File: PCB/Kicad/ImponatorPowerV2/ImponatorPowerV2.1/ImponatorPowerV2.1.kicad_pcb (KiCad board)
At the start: 6 copper layers, 79 parts, among them IC1 IS31FL3728-QFLS2-TR

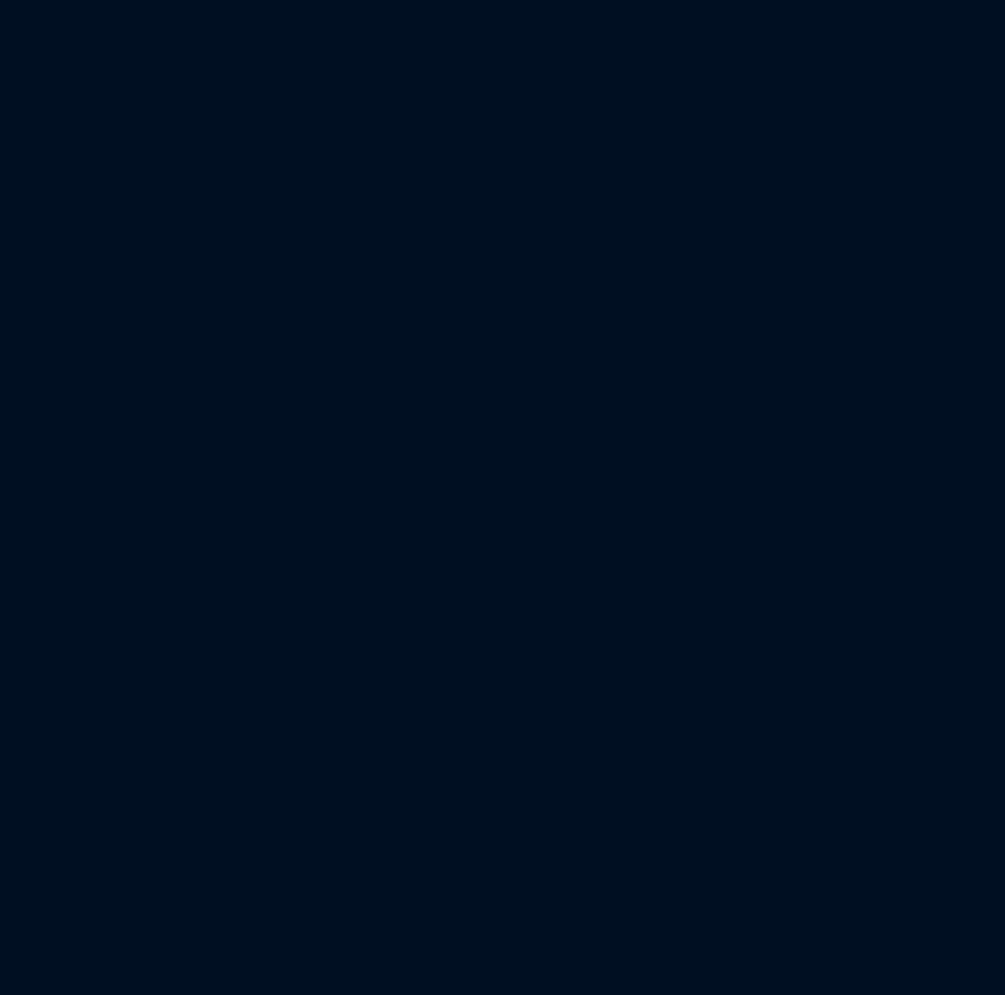
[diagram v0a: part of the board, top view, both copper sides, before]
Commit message: Added components to PCB on V2.1
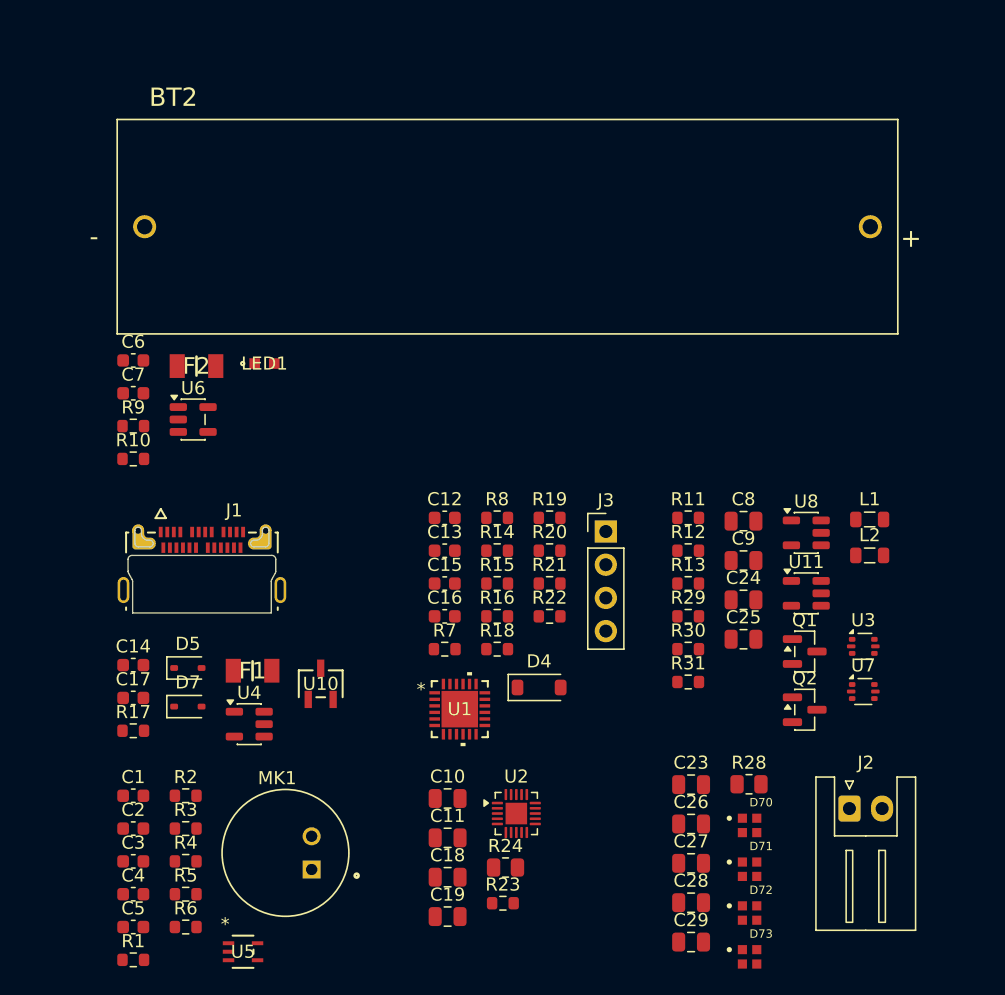
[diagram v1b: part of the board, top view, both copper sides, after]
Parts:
- added BT2: BCAAPC, Custom:BAT_BCAAPC, F.Cu at (94.1, 98.5)
- added C1: 0.1uF, Capacitor_SMD:C_0603_1608Metric, F.Cu at (65.5, 142.0)
- added C10: 4.7uF, Capacitor_SMD:C_0805_2012Metric, F.Cu at (89.5, 142.3)
- added C11: 0.1uF, Capacitor_SMD:C_0805_2012Metric, F.Cu at (89.5, 145.3)
- added C12: 1uF, Capacitor_SMD:C_0603_1608Metric, F.Cu at (89.3, 120.8)
- added C13: 100nF, Capacitor_SMD:C_0603_1608Metric, F.Cu at (89.3, 123.3)
- added C14: 4.7uF, Capacitor_SMD:C_0603_1608Metric, F.Cu at (65.5, 132.1)
- added C15: 1uF, Capacitor_SMD:C_0603_1608Metric, F.Cu at (89.3, 125.8)
- added C16: 1uF, Capacitor_SMD:C_0603_1608Metric, F.Cu at (89.3, 128.3)
- added C17: 1uF, Capacitor_SMD:C_0603_1608Metric, F.Cu at (65.5, 134.6)
- added C18: 4.7uF, Capacitor_SMD:C_0805_2012Metric, F.Cu at (89.5, 148.3)
- added C19: 0.1uF, Capacitor_SMD:C_0805_2012Metric, F.Cu at (89.5, 151.3)
- added C2: 1uF, Capacitor_SMD:C_0603_1608Metric, F.Cu at (65.5, 144.6)
- added C23: 0.1uF, Capacitor_SMD:C_0805_2012Metric, F.Cu at (108.2, 141.2)
- added C24: 4.7uF, Capacitor_SMD:C_0805_2012Metric, F.Cu at (112.2, 127.1)
- added C25: 22uF, Capacitor_SMD:C_0805_2012Metric, F.Cu at (112.2, 130.1)
- added C26: 0.1uF, Capacitor_SMD:C_0805_2012Metric, F.Cu at (108.2, 144.2)
- added C27: 0.1uF, Capacitor_SMD:C_0805_2012Metric, F.Cu at (108.2, 147.2)
- added C28: 0.1uF, Capacitor_SMD:C_0805_2012Metric, F.Cu at (108.2, 150.2)
- added C29: 100uF, Capacitor_SMD:C_0805_2012Metric, F.Cu at (108.2, 153.2)
- added C3: 100pF, Capacitor_SMD:C_0603_1608Metric, F.Cu at (65.5, 147.1)
- added C4: 1uF, Capacitor_SMD:C_0603_1608Metric, F.Cu at (65.5, 149.6)
- added C5: 0.1uF, Capacitor_SMD:C_0603_1608Metric, F.Cu at (65.5, 152.1)
- added C6: 4.7uF, Capacitor_SMD:C_0603_1608Metric, F.Cu at (65.5, 108.8)
- added C7: 4.7uF, Capacitor_SMD:C_0603_1608Metric, F.Cu at (65.5, 111.3)
- added C8: 4.7uF, Capacitor_SMD:C_0805_2012Metric, F.Cu at (112.2, 121.0)
- added C9: 22uF, Capacitor_SMD:C_0805_2012Metric, F.Cu at (112.2, 124.1)
- added D4: BZT52B5V1, Diode_SMD:D_SOD-123, F.Cu at (96.5, 133.8)
- added D5: ESDSB5V0D3BHE3, Diode_SMD:D_SOD-323, F.Cu at (69.7, 132.3)
- added D7: ESDSB5V0D3BHE3, Diode_SMD:D_SOD-323, F.Cu at (69.7, 135.2)
- added D70: SMD-LX0707RGB-TR, Custom:LED_SMD-LX0707RGB-TR, F.Cu at (112.6, 144.3)
- added D71: SMD-LX0707RGB-TR, Custom:LED_SMD-LX0707RGB-TR, F.Cu at (112.6, 147.7)
- added D72: SMD-LX0707RGB-TR, Custom:LED_SMD-LX0707RGB-TR, F.Cu at (112.6, 151.0)
- added D73: SMD-LX0707RGB-TR, Custom:LED_SMD-LX0707RGB-TR, F.Cu at (112.6, 154.4)
- added F1: 1206L150THWR, custom2:FUSC3216X100N, F.Cu at (74.6, 132.5)
- added F2: 1206L150THWR, custom2:FUSC3216X100N, F.Cu at (70.3, 109.2)
- added J1: USB type-c, Custom:MOLEX_2024100002, F.Cu at (70.8, 128.1)
- added J2: Conn_01x02, Connector_JST:JST_XH_S2B-XH-A_1x02_P2.50mm_Horizontal, F.Cu at (120.3, 143.0)
- added J3: Conn_01x04_Pin, Connector_PinHeader_2.54mm:PinHeader_1x04_P2.54mm_Vertical, F.Cu at (101.6, 121.8)
- added L1: 1.0uH, Inductor_SMD:L_0805_2012Metric, F.Cu at (121.8, 120.9)
- added L2: 1.0uH, Inductor_SMD:L_0805_2012Metric, F.Cu at (121.8, 123.7)
- added LED1: LTST-C190KFKT, Custom:LED_LSTS-C190_LTO, F.Cu at (75.5, 109.0)
- added MK1: CMA-4544PF-W, Custom:MIC_CMA-4544PF-W, F.Cu at (77.1, 146.4)
- added Q1: AO3400A, Custom:UMW A03400A, F.Cu at (116.9, 131.0)
- added Q2: AO3400A, Custom:UMW A03400A, F.Cu at (116.9, 135.5)
- added R1: 2k, Resistor_SMD:R_0603_1608Metric, F.Cu at (65.5, 154.6)
- added R10: 2K, Resistor_SMD:R_0603_1608Metric, F.Cu at (65.5, 116.3)
- added R11: 604K, Resistor_SMD:R_0603_1608Metric, F.Cu at (107.9, 120.8)
- added R12: 82K, Resistor_SMD:R_0603_1608Metric, F.Cu at (107.9, 123.3)
- added R13: 499K, Resistor_SMD:R_0603_1608Metric, F.Cu at (107.9, 125.8)
- added R14: 22K, Resistor_SMD:R_0603_1608Metric, F.Cu at (93.3, 123.3)
- added R15: 100K, Resistor_SMD:R_0603_1608Metric, F.Cu at (93.3, 125.8)
- added R16: 10K, Resistor_SMD:R_0603_1608Metric, F.Cu at (93.3, 128.3)
- added R17: 1K, Resistor_SMD:R_0603_1608Metric, F.Cu at (65.5, 137.1)
- added R18: 100K, Resistor_SMD:R_0603_1608Metric, F.Cu at (93.3, 130.8)
- added R19: 100R, Resistor_SMD:R_0603_1608Metric, F.Cu at (97.3, 120.8)
- added R2: 2k, Resistor_SMD:R_0603_1608Metric, F.Cu at (69.5, 142.0)
- added R20: 22R, Resistor_SMD:R_0603_1608Metric, F.Cu at (97.3, 123.3)
- added R21: 100K, Resistor_SMD:R_0603_1608Metric, F.Cu at (97.3, 125.8)
- added R22: 100K, Resistor_SMD:R_0603_1608Metric, F.Cu at (97.3, 128.3)
- added R23: 4.7K, Resistor_SMD:R_0603_1608Metric, F.Cu at (93.8, 150.3)
- added R24: 0R, Custom:RST, F.Cu at (94.0, 147.5)
- added R28: 330R, Resistor_SMD:R_0805_2012Metric, F.Cu at (112.6, 141.2)
- added R29: 499K, Resistor_SMD:R_0603_1608Metric, F.Cu at (107.9, 128.3)
- added R3: 100k, Resistor_SMD:R_0603_1608Metric, F.Cu at (69.5, 144.6)
- added R30: 369K, Resistor_SMD:R_0603_1608Metric, F.Cu at (107.9, 130.8)
- added R31: 82K, Resistor_SMD:R_0603_1608Metric, F.Cu at (107.9, 133.3)
- added R4: 100k, Resistor_SMD:R_0603_1608Metric, F.Cu at (69.5, 147.1)
- added R5: 100k, Resistor_SMD:R_0603_1608Metric, F.Cu at (69.5, 149.6)
- added R6: 3.3k, Resistor_SMD:R_0603_1608Metric, F.Cu at (69.5, 152.1)
- added R7: 470R, Resistor_SMD:R_0603_1608Metric, F.Cu at (89.3, 130.8)
- added R8: 1K, Resistor_SMD:R_0603_1608Metric, F.Cu at (93.3, 120.8)
- added R9: 470, Resistor_SMD:R_0603_1608Metric, F.Cu at (65.5, 113.8)
- added U1: STUSB4500QTR, Custom:QFN24EP_4X4_STM, F.Cu at (90.5, 135.4)
- added U10: AO3401A, Custom:SOT-23-3L_AOS, F.Cu at (79.8, 133.5)
- added U11: ACS37041, Custom:ACS37041KLHBLT-010B5, F.Cu at (117.0, 126.6)
- added U2: EFM8UB10F16G, Package_DFN_QFN:QFN-20-1EP_3x3mm_P0.4mm_EP1.65x1.65mm, F.Cu at (94.8, 143.4)
- added U3: TPS62A01DRLR, Package_TO_SOT_SMD:SOT-666, F.Cu at (121.3, 130.6)
- added U4: ACS37041, Custom:ACS37041KLHBLT-010B5, F.Cu at (74.4, 136.6)
- added U5: MAX4466EXK+T, Custom:21-0076E_MXM, F.Cu at (73.9, 154.0)
- added U6: MCP73831T-2ACI/OT, Package_TO_SOT_SMD:SOT-23-5, F.Cu at (70.1, 113.3)
- added U7: TPS62A01DRLR, Package_TO_SOT_SMD:SOT-666, F.Cu at (121.3, 134.1)
- added U8: ACS37041, Custom:ACS37041KLHBLT-010B5, F.Cu at (117.0, 121.9)
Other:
- board outline added: 11.3 x 6.6 mm

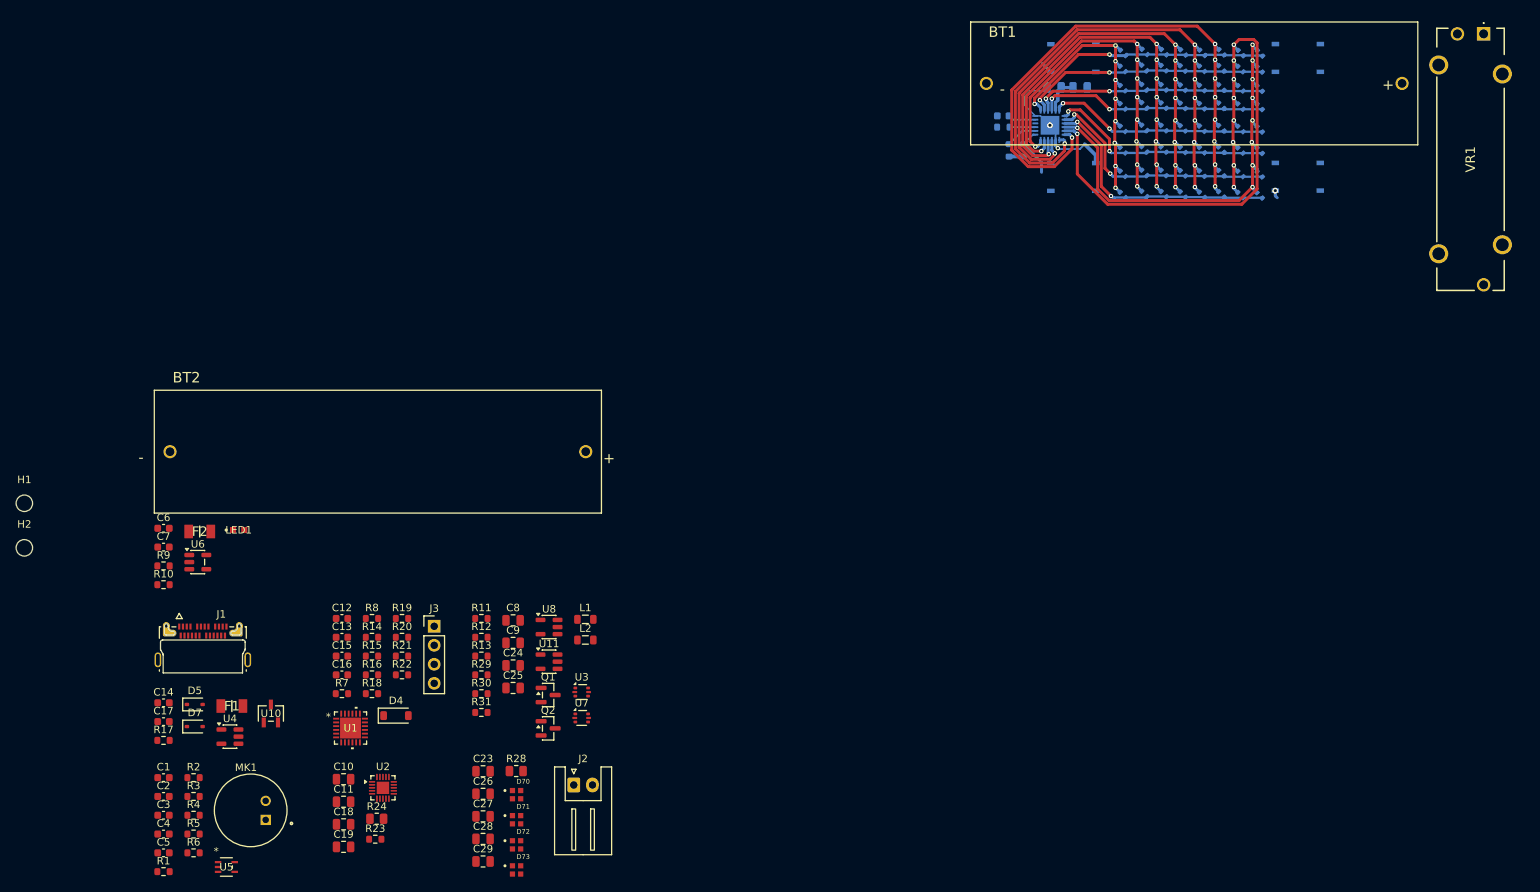
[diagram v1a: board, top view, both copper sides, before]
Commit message: 6 layer version of imponatorPower routed.
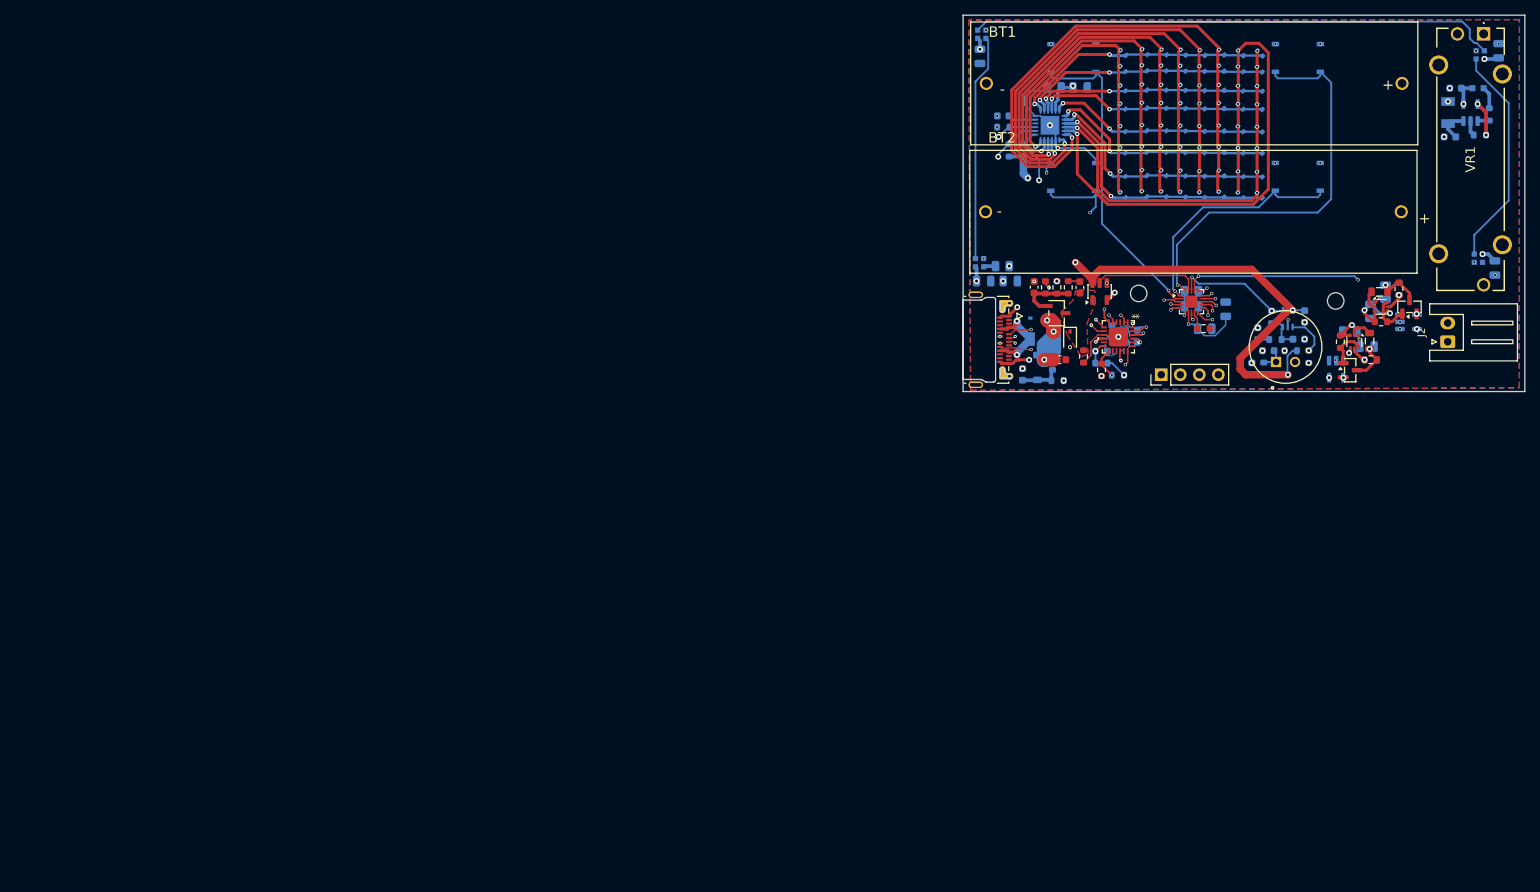
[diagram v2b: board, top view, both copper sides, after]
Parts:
- removed R24: 0R, Custom:RST
- C1, C10, C11, C12, C15, C16, C18, C19, C2, C23, C24, C25, C26, C27, C28, C29, C3, C4, C5, C6, C7, C8, C9, D4, D5, D70, D71, D72, D73, F1, F2, LED1, R1, R10, R12, R16, R18, R2, R20, R21, R28, R3, R31, R4, R5, R6, R7, R8, R9, U11, U5, U6, U8: moved to B.Cu
- moved R9 187.0 mm to (242.5, 53.5), turned to -90 degrees
- moved R10 185.7 mm to (241.2, 56.2), turned to 180 degrees
- moved C6 182.2 mm to (238.0, 50.0)
- moved C7 180.3 mm to (237.2, 56.5)
- moved U6 180.2 mm to (240.0, 53.2), turned to 90 degrees
- moved H2 178.2 mm to (222.0, 78.4)
- moved F2 175.8 mm to (237.0, 53.2), turned to 90 degrees
- moved LED1 175.7 mm to (241.0, 50.0), turned to 180 degrees
- moved C27 169.8 mm to (243.8, 45.0), turned to -90 degrees
- moved C5 168.3 mm to (217.8, 80.5), turned to 90 degrees
- moved D72 166.4 mm to (241.3, 45.5)
- moved C3 164.4 mm to (217.1, 83.5), turned to 180 degrees
- moved R1 161.5 mm to (212.4, 87.5), turned to -90 degrees
- moved R4 161.0 mm to (218.4, 85.8), turned to 90 degrees
- moved C4 160.6 mm to (211.6, 82.8), turned to 90 degrees
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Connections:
- R23 pad 2: Net-(R23-Pad2) -> GND
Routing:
- net +5VBat: track 0.00 -> 225.3 mm, vias 0 -> 7
- net +3V3Bat: track 7.06 -> 136.0 mm, vias 0 -> 6
- net V_bat: track 0.00 -> 89.8 mm, vias 0 -> 5
- net /Microcontroller/Slider: track 0.00 -> 81.2 mm, vias 0 -> 1
- net Net-(D71-DOUT): track 0.00 -> 70.5 mm
- net +5V: track 0.00 -> 69.5 mm, vias 0 -> 2
- net /USB/VBUS: track 0.00 -> 58.3 mm, vias 0 -> 5
- net /Microcontroller/Previous_btn: track 0.00 -> 54.9 mm, vias 0 -> 1
- net /Microcontroller/SCL: track 4.54 -> 58.1 mm, vias 0 -> 2
- net /Microcontroller/Matrix Switch: track 3.45 -> 53.3 mm, vias 0 -> 2
- net /Microcontroller/SDA: track 6.88 -> 48.4 mm, vias 0 -> 2
- net /Microcontroller/CTM1_btn: track 1.71 -> 42.8 mm, vias 0 -> 1
- net GND: track 20.8 -> 56.0 mm, vias 2 -> 38
- net /Microcontroller/CTM2_btn: track 0.23 -> 32.9 mm, vias 0 -> 2
- net 5VBat_current: track 0.00 -> 32.2 mm, vias 0 -> 3
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- added copper zone on F.Cu, net /USB/Drain
- added copper zone on B.Cu, net GND
- added copper zone on F.Cu, net GND
- added copper zone on In1.Cu, net GND
- added copper zone on In4.Cu, net GND
- added copper zone on In3.Cu, net V_bat
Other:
- board size 11.3 x 6.6 mm -> 75 x 50.2 mm

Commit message: Fixed corrupted readmes, added some drawing to ImponatorPower V2.1 Silkscreen and made an readme for ImponatorPower V2.1 with added images of the PCB layout.
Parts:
- added G***: LOGO, LOGO, B.Cu at (226.0, 64.8)
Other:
- board text added: "Trym .F Imponator greie V3"
